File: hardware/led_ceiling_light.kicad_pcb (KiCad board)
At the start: 2 copper layers, 95 x 50 mm, 22 parts, among them J1 Screw_Terminal_01x03, Q1 BSS123, U1 AL8861

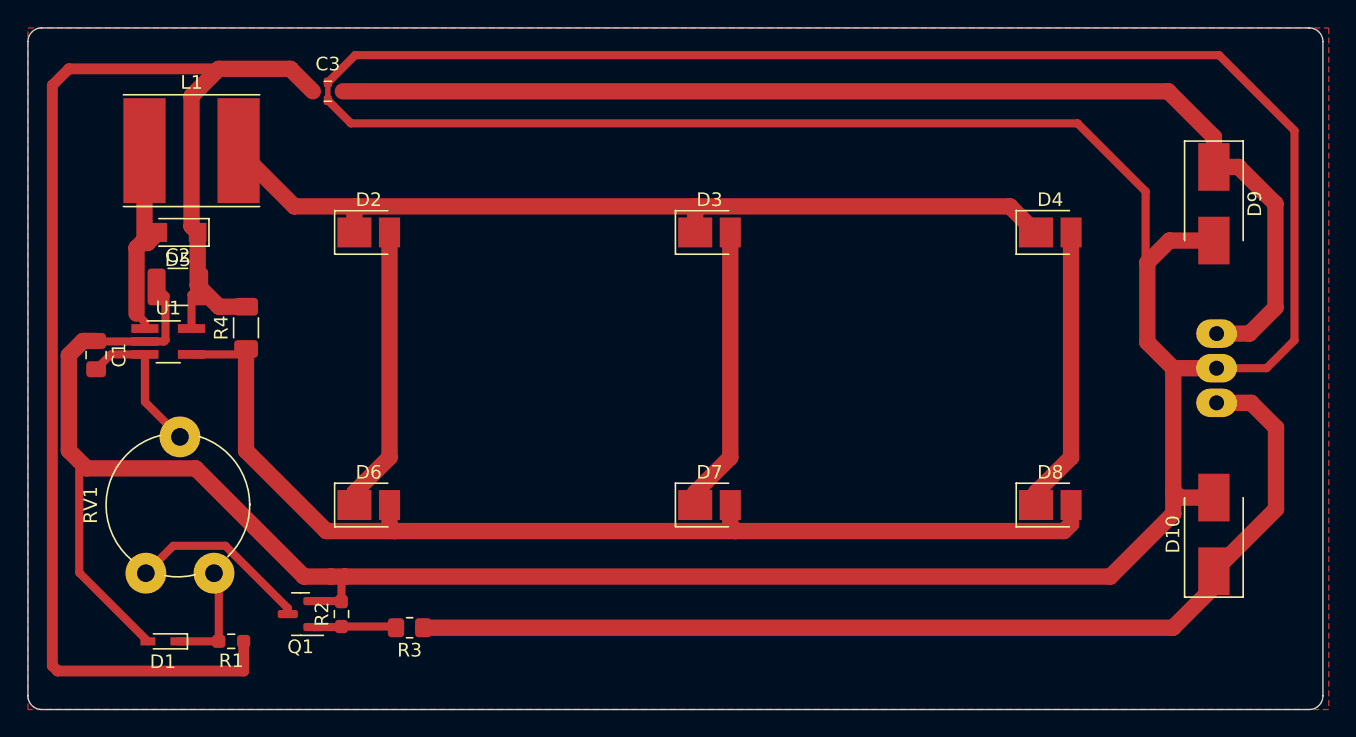
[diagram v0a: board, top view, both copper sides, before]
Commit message: Add optional a 3rd LED in serie (so we can have a 3x2 or 3x3 matrix). Re-annotate whole schematic
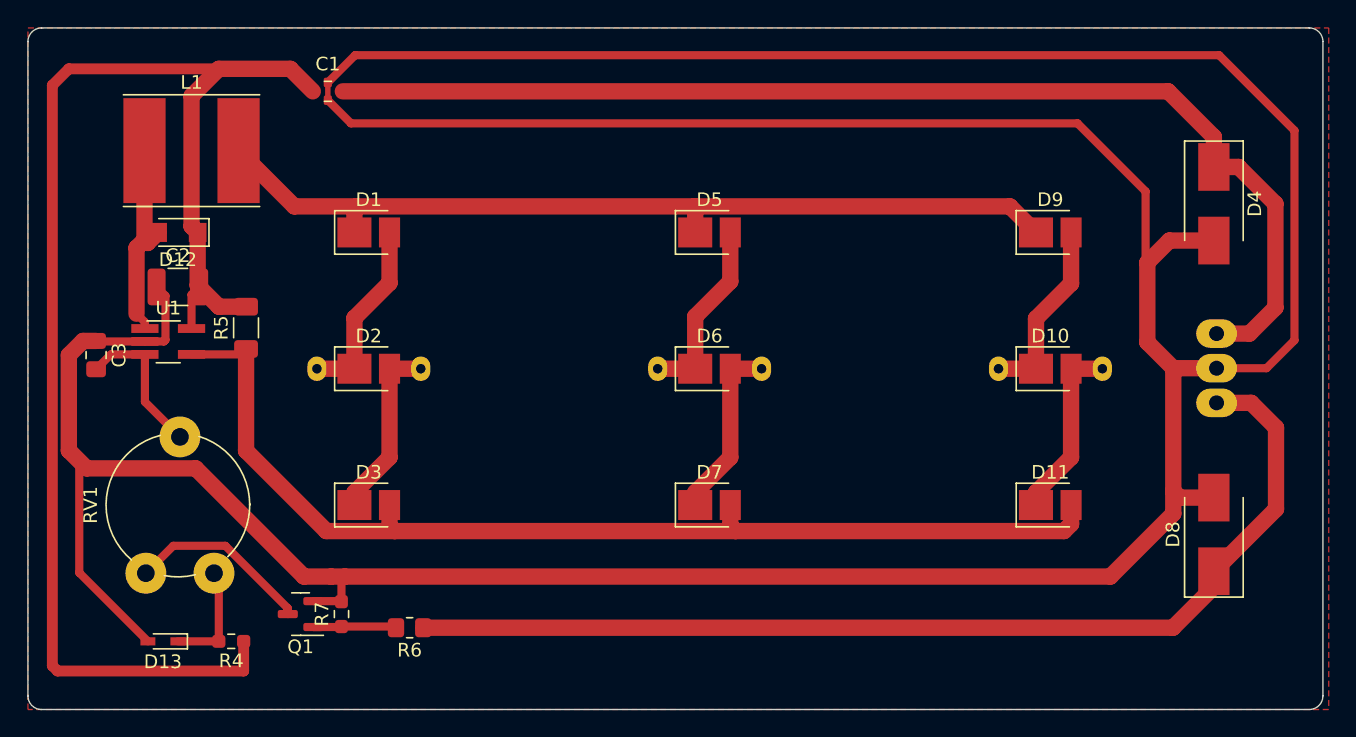
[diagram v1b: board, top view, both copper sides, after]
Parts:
- added D10: N/A, LED_SMD:LED_PLCC_2835_Handsoldering, F.Cu at (175.0, 85.0)
- added D2: N/A, LED_SMD:LED_PLCC_2835_Handsoldering, F.Cu at (125.0, 85.0)
- added D6: N/A, LED_SMD:LED_PLCC_2835_Handsoldering, F.Cu at (150.0, 85.0)
- added R1: 0, Resistor_THT:R_Axial_DIN0204_L3.6mm_D1.6mm_P7.62mm_Horizontal, B.Cu at (121.2, 85.0)
- added R2: 0, Resistor_THT:R_Axial_DIN0204_L3.6mm_D1.6mm_P7.62mm_Horizontal, B.Cu at (146.2, 85.0)
- added R3: 0, Resistor_THT:R_Axial_DIN0204_L3.6mm_D1.6mm_P7.62mm_Horizontal, B.Cu at (171.2, 85.0)
- renumbered C3 to C1, C1 to C3, D2 to D1, D8 to D11, D5 to D12, D1 to D13, D6 to D3, D9 to D4, D3 to D5, D10 to D8, D4 to D9, R1 to R4, R4 to R5, R3 to R6, R2 to R7
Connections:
- D1 pad 2: Net-(D2-Pad2) -> Net-(D1-Pad2)
- D11 pad 1: Net-(D4-Pad2) -> Net-(D10-Pad2)
- D5 pad 2: Net-(D3-Pad2) -> Net-(D5-Pad2)
- D7 pad 1: Net-(D3-Pad2) -> Net-(D6-Pad2)
- D9 pad 2: Net-(D4-Pad2) -> Net-(D10-Pad1)
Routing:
- net Net-(D4-Pad2): track 21.1 -> 0.00 mm
- net Net-(D3-Pad2): track 21.1 -> 0.00 mm
- net Net-(D10-Pad1): track 0.00 -> 13.8 mm
- net Net-(D5-Pad2): track 0.00 -> 13.8 mm
- net Net-(D1-Pad2): track 0.00 -> 13.8 mm
- net Net-(D6-Pad2): track 0.00 -> 13.4 mm
- net Net-(D10-Pad2): track 0.00 -> 13.4 mm
- net Net-(D2-Pad2): track 21.1 -> 13.4 mm
- net Net-(D8-Pad1): track 77.9 -> 76.8 mm

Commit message: Cosmetic adjust tracks
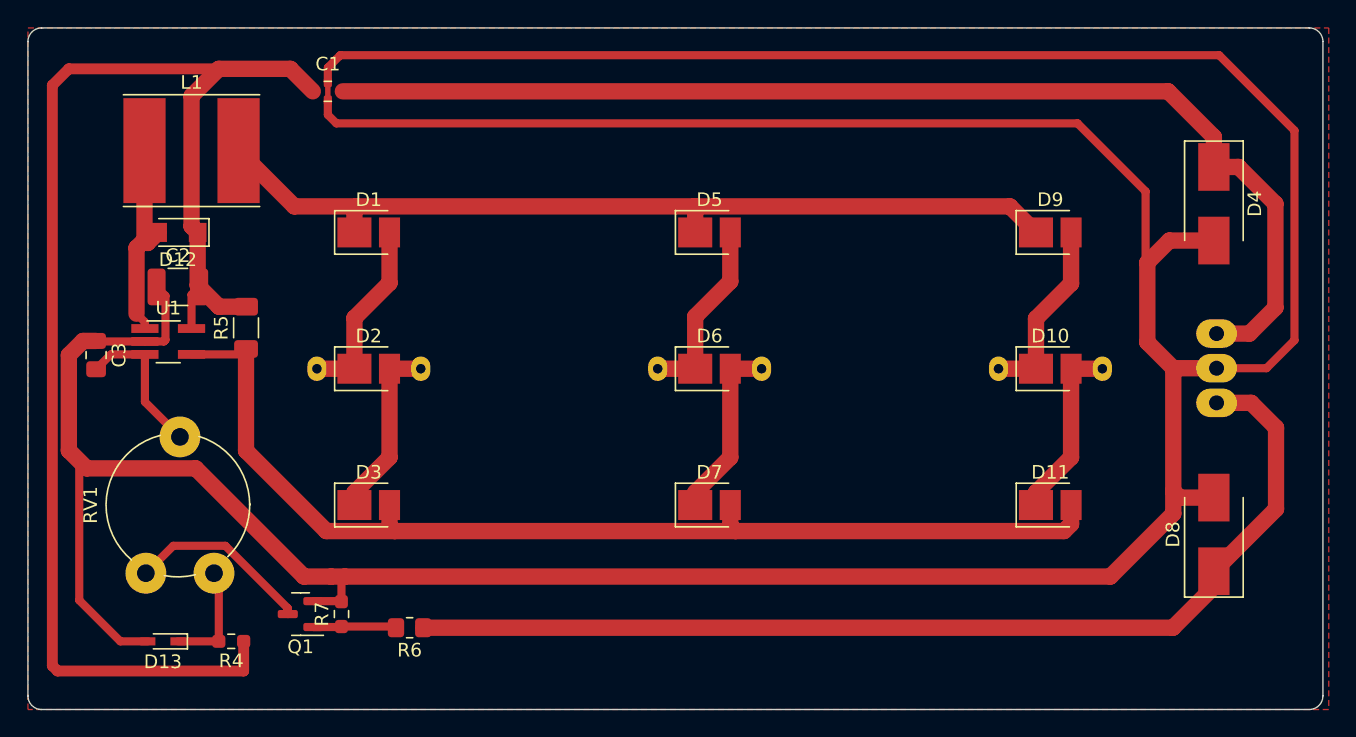
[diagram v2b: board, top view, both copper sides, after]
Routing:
- net GND: track 326.7 -> 329.1 mm
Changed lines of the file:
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@@
   (segment (start 120.9375 102.05) (end 122.9625 102.05) (width 0.6) (layer "F.Cu") (net 1))
   (segment (start 104.0375 82.9625) (end 105 82.9625) (width 1.2) (layer "F.Cu") (net 1))
-  (segment (start 123.7 67) (end 122 65.3) (width 0.6) (layer "F.Cu") (net 1))
-  (segment (start 192.913 82.913) (end 190.863 84.963) (width 0.6) (layer "F.Cu") (net 1))
+  (segment (start 122.246361 100.246361) (end 120.246361 100.246361) (width 1.2) (layer "F.Cu") (net 1))
+  (segment (start 181.991 81.7) (end 181.991 71.991) (width 0.6) (layer "F.Cu") (net 1))
   (segment (start 190.863 84.963) (end 187.198 84.963) (width 0.6) (layer "F.Cu") (net 1))
-  (segment (start 122.246361 100.246361) (end 120.246361 100.246361) (width 1.2) (layer "F.Cu") (net 1))
+  (segment (start 122.912 62) (end 187.3885 62) (width 0.6) (layer "F.Cu") (net 1))
   (segment (start 179.407639 100.246361) (end 123.246361 100.246361) (width 1.2) (layer "F.Cu") (net 1))
   (segment (start 182.118 83.058) (end 184.023 84.963) (width 1.2) (layer "F.Cu") (net 1))
   (segment (start 184.023 95.631) (end 179.407639 100.246361) (width 1.2) (layer "F.Cu") (net 1))
-  (segment (start 181.991 71.991) (end 177 67) (width 0.6) (layer "F.Cu") (net 1))
+  (segment (start 177 67) (end 122.626 67) (width 0.6) (layer "F.Cu") (net 1))
   (segment (start 108.58 83) (end 105.0375 83) (width 0.6) (layer "F.Cu") (net 1))
   (segment (start 110.09 82.885) (end 110.09 79.6525) (width 0.6) (layer "F.Cu") (net 1))
   (segment (start 103 91) (end 103 84) (width 1.2) (layer "F.Cu") (net 1))
-  (segment (start 103.765 91.765) (end 103 91) (width 0.6) (layer "F.Cu") (net 1))
-  (segment (start 181.991 81.7) (end 181.991 71.991) (width 0.6) (layer "F.Cu") (net 1))
-  (segment (start 103.765 99.965) (end 103.765 91.765) (width 0.6) (layer "F.Cu") (net 1))
+  (segment (start 106.778 105) (end 103.765 101.987) (width 0.6) (layer "F.Cu") (net 1))
+  (segment (start 187.3885 62) (end 192.913 67.5245) (width 0.6) (layer "F.Cu") (net 1))
+  (segment (start 122 64) (end 122 62.912) (width 0.6) (layer "F.Cu") (net 1))
   (segment (start 104.31 92.31) (end 103 91) (width 1.2) (layer "F.Cu") (net 1))
   (segment (start 184.023 84.963) (end 187.198 84.963) (width 1.2) (layer "F.Cu") (net 1))
   (segment (start 122 65.3) (end 122 64) (width 0.4) (layer "F.Cu") (net 1))
+  (segment (start 122 66.374) (end 122 65.3) (width 0.6) (layer "F.Cu") (net 1))
   (segment (start 182.118 77.216) (end 182.118 83.058) (width 1.2) (layer "F.Cu") (net 1))
   (segment (start 123 102.0875) (end 123 100.492722) (width 0.6) (layer "F.Cu") (net 1))
-  (segment (start 124 62) (end 187.3885 62) (width 0.6) (layer "F.Cu") (net 1))
   (segment (start 123.246361 100.246361) (end 122.246361 100.246361) (width 1.2) (layer "F.Cu") (net 1))
+  (segment (start 108.8 105) (end 106.778 105) (width 0.6) (layer "F.Cu") (net 1))
+  (segment (start 122 62.912) (end 122.912 62) (width 0.6) (layer "F.Cu") (net 1))
   (segment (start 103 84) (end 104.0375 82.9625) (width 1.2) (layer "F.Cu") (net 1))
   (segment (start 187 94.455) (end 184.498 94.455) (width 1.2) (layer "F.Cu") (net 1))
   (segment (start 109.975 83) (end 110.09 82.885) (width 0.6) (layer "F.Cu") (net 1))
   (segment (start 112.31 92.31) (end 104.31 92.31) (width 1.2) (layer "F.Cu") (net 1))
-  (segment (start 187.3885 62) (end 192.913 67.5245) (width 0.6) (layer "F.Cu") (net 1))
+  (segment (start 192.913 82.913) (end 190.863 84.963) (width 0.6) (layer "F.Cu") (net 1))
   (segment (start 187 75.598) (end 183.736 75.598) (width 1.2) (layer "F.Cu") (net 1))
   (segment (start 120.246361 100.246361) (end 112.31 92.31) (width 1.2) (layer "F.Cu") (net 1))
-  (segment (start 108.8 105) (end 103.765 99.965) (width 0.6) (layer "F.Cu") (net 1))
   (segment (start 123 100.492722) (end 123.246361 100.246361) (width 0.6) (layer "F.Cu") (net 1))
-  (segment (start 122 64) (end 124 62) (width 0.6) (layer "F.Cu") (net 1))
+  (segment (start 103.765 91.765) (end 103 91) (width 0.6) (layer "F.Cu") (net 1))
+  (segment (start 122.626 67) (end 122 66.374) (width 0.6) (layer "F.Cu") (net 1))
   (segment (start 192.913 67.5245) (end 192.913 82.913) (width 0.6) (layer "F.Cu") (net 1))
   (segment (start 108.58 83) (end 109.975 83) (width 0.6) (layer "F.Cu") (net 1))
@@
   (segment (start 184.023 84.963) (end 184.023 93.98) (width 1.2) (layer "F.Cu") (net 1))
   (segment (start 184.023 93.98) (end 184.023 95.631) (width 1.2) (layer "F.Cu") (net 1))
+  (segment (start 103.765 101.987) (end 103.765 91.765) (width 0.6) (layer "F.Cu") (net 1))
   (segment (start 183.736 75.598) (end 182.118 77.216) (width 1.2) (layer "F.Cu") (net 1))
   (segment (start 110.09 79.6525) (end 109.4375 79) (width 0.6) (layer "F.Cu") (net 1))
-  (segment (start 177 67) (end 123.7 67) (width 0.6) (layer "F.Cu") (net 1))
+  (segment (start 181.991 71.991) (end 177 67) (width 0.6) (layer "F.Cu") (net 1))
   (segment (start 187 68) (end 183.65 64.65) (width 1.2) (layer "F.Cu") (net 2))
   (segment (start 191.516 80.518) (end 189.611 82.423) (width 1.2) (layer "F.Cu") (net 2))
